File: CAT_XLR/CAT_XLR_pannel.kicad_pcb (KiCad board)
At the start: 2 copper layers, 94 x 120 mm, 92 parts, among them J0 8P8C_Shielded, J1 XLR5, J2 XLR5, J3 XLR5, J4 XLR5, J5 XLR5, J6 XLR5, J7 XLR5, J8 XLR5

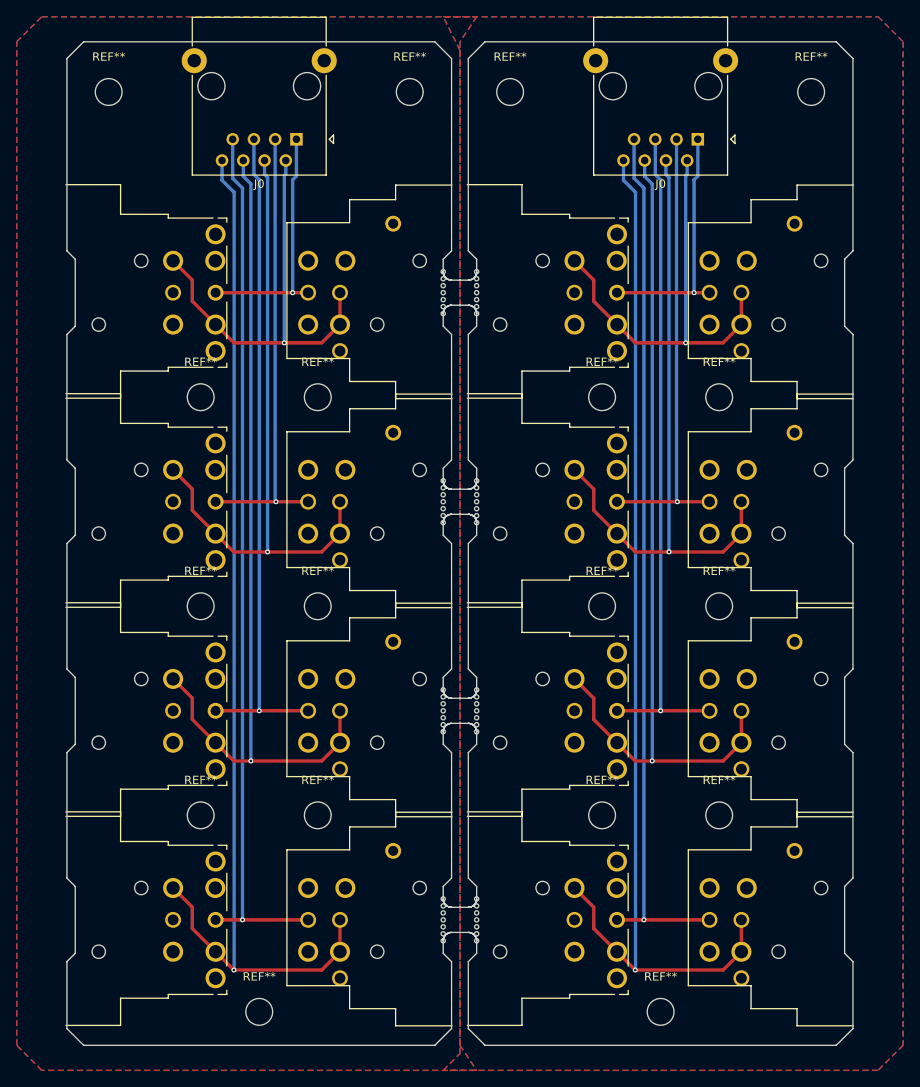
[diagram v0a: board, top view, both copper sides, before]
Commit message: fixed CAT connection and gnd connection
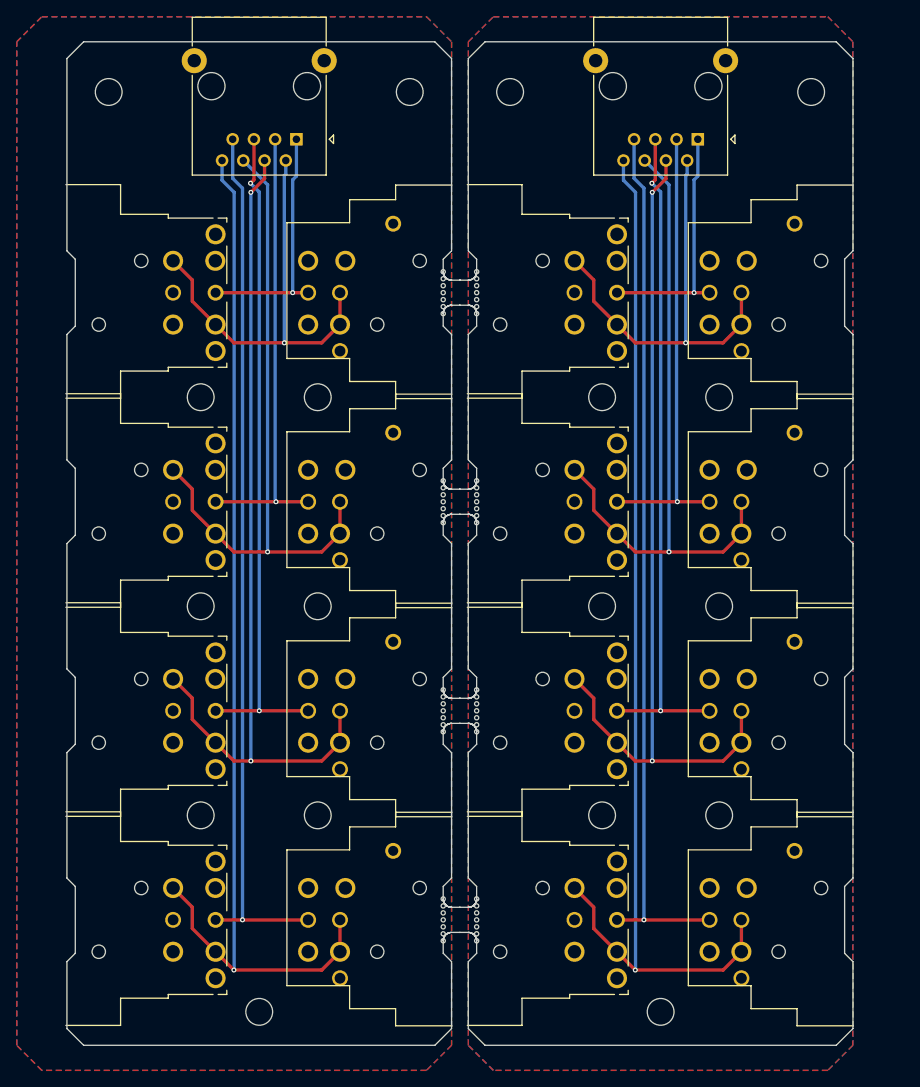
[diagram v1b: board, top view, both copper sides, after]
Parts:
- removed REF** (x18): MountingHole_3.2mm_M3, MountingHole:MountingHole_3.2mm_M3
- added ?: MountingHole_3.2mm_M3, MountingHole:MountingHole_3.2mm_M3, F.Cu at (106.5, 26.0)
- added ?: MountingHole_3.2mm_M3, MountingHole:MountingHole_3.2mm_M3, F.Cu at (179.5, 87.5)
- added ?: MountingHole_3.2mm_M3, MountingHole:MountingHole_3.2mm_M3, F.Cu at (154.5, 26.0)
- added ?: MountingHole_3.2mm_M3, MountingHole:MountingHole_3.2mm_M3, F.Cu at (165.5, 62.5)
- added ?: MountingHole_3.2mm_M3, MountingHole:MountingHole_3.2mm_M3, F.Cu at (172.5, 136.0)
- added ?: MountingHole_3.2mm_M3, MountingHole:MountingHole_3.2mm_M3, F.Cu at (165.5, 87.5)
- added ?: MountingHole_3.2mm_M3, MountingHole:MountingHole_3.2mm_M3, F.Cu at (131.5, 87.5)
- added ?: MountingHole_3.2mm_M3, MountingHole:MountingHole_3.2mm_M3, F.Cu at (142.5, 26.0)
- added ?: MountingHole_3.2mm_M3, MountingHole:MountingHole_3.2mm_M3, F.Cu at (179.5, 112.5)
- added ?: MountingHole_3.2mm_M3, MountingHole:MountingHole_3.2mm_M3, F.Cu at (117.5, 87.5)
- added ?: MountingHole_3.2mm_M3, MountingHole:MountingHole_3.2mm_M3, F.Cu at (179.5, 62.5)
- added ?: MountingHole_3.2mm_M3, MountingHole:MountingHole_3.2mm_M3, F.Cu at (190.5, 26.0)
- added ?: MountingHole_3.2mm_M3, MountingHole:MountingHole_3.2mm_M3, F.Cu at (117.5, 112.5)
- added ?: MountingHole_3.2mm_M3, MountingHole:MountingHole_3.2mm_M3, F.Cu at (131.5, 62.5)
- added ?: MountingHole_3.2mm_M3, MountingHole:MountingHole_3.2mm_M3, F.Cu at (124.5, 136.0)
- added ?: MountingHole_3.2mm_M3, MountingHole:MountingHole_3.2mm_M3, F.Cu at (165.5, 112.5)
- added ?: MountingHole_3.2mm_M3, MountingHole:MountingHole_3.2mm_M3, F.Cu at (117.5, 62.5)
- added ?: MountingHole_3.2mm_M3, MountingHole:MountingHole_3.2mm_M3, F.Cu at (131.5, 112.5)
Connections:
- J0 pad 4: Board_0-DATA- 2 -> Board_0-DATA- 3
- J0 pad 6: Board_0-DATA- 3 -> Board_0-DATA- 2
- J0 pad 4: Board_1-DATA- 2 -> Board_1-DATA- 3
- J0 pad 6: Board_1-DATA- 3 -> Board_1-DATA- 2
- J1 pad G: (no net) -> Board_1-GND
- J1 pad G: (no net) -> Board_0-GND
- J2 pad G: (no net) -> Board_0-GND
- J2 pad G: (no net) -> Board_1-GND
- J3 pad G: (no net) -> Board_1-GND
- J3 pad G: (no net) -> Board_0-GND
- J4 pad G: (no net) -> Board_0-GND
- J4 pad G: (no net) -> Board_1-GND
- J5 pad G: (no net) -> Board_0-GND
- J5 pad G: (no net) -> Board_1-GND
- J6 pad G: (no net) -> Board_0-GND
- J6 pad G: (no net) -> Board_1-GND
- J7 pad G: (no net) -> Board_1-GND
- J7 pad G: (no net) -> Board_0-GND
- J8 pad G: (no net) -> Board_0-GND
- J8 pad G: (no net) -> Board_1-GND
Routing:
- net Board_1-DATA- 2: track 77.2 -> 78.4 mm
- net Board_0-DATA- 2: track 77.2 -> 78.4 mm
- net Board_1-DATA+ 3: track 79.7 -> 80.0 mm, vias 1 -> 2
- net Board_0-DATA+ 3: track 79.7 -> 80.0 mm, vias 1 -> 2
- net Board_0-DATA- 3: track 102.4 -> 102.7 mm, vias 1 -> 2
- net Board_1-DATA- 3: track 102.4 -> 102.7 mm, vias 1 -> 2
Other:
- board text removed: "PREVIEW ONLY. PANEL SAVED IN /home/jakob/KiCad/ShowControllPCBs/CAT_XLR/CAT_XLR_pannel.kicad_pcb"
